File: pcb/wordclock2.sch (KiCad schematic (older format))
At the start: 42 parts

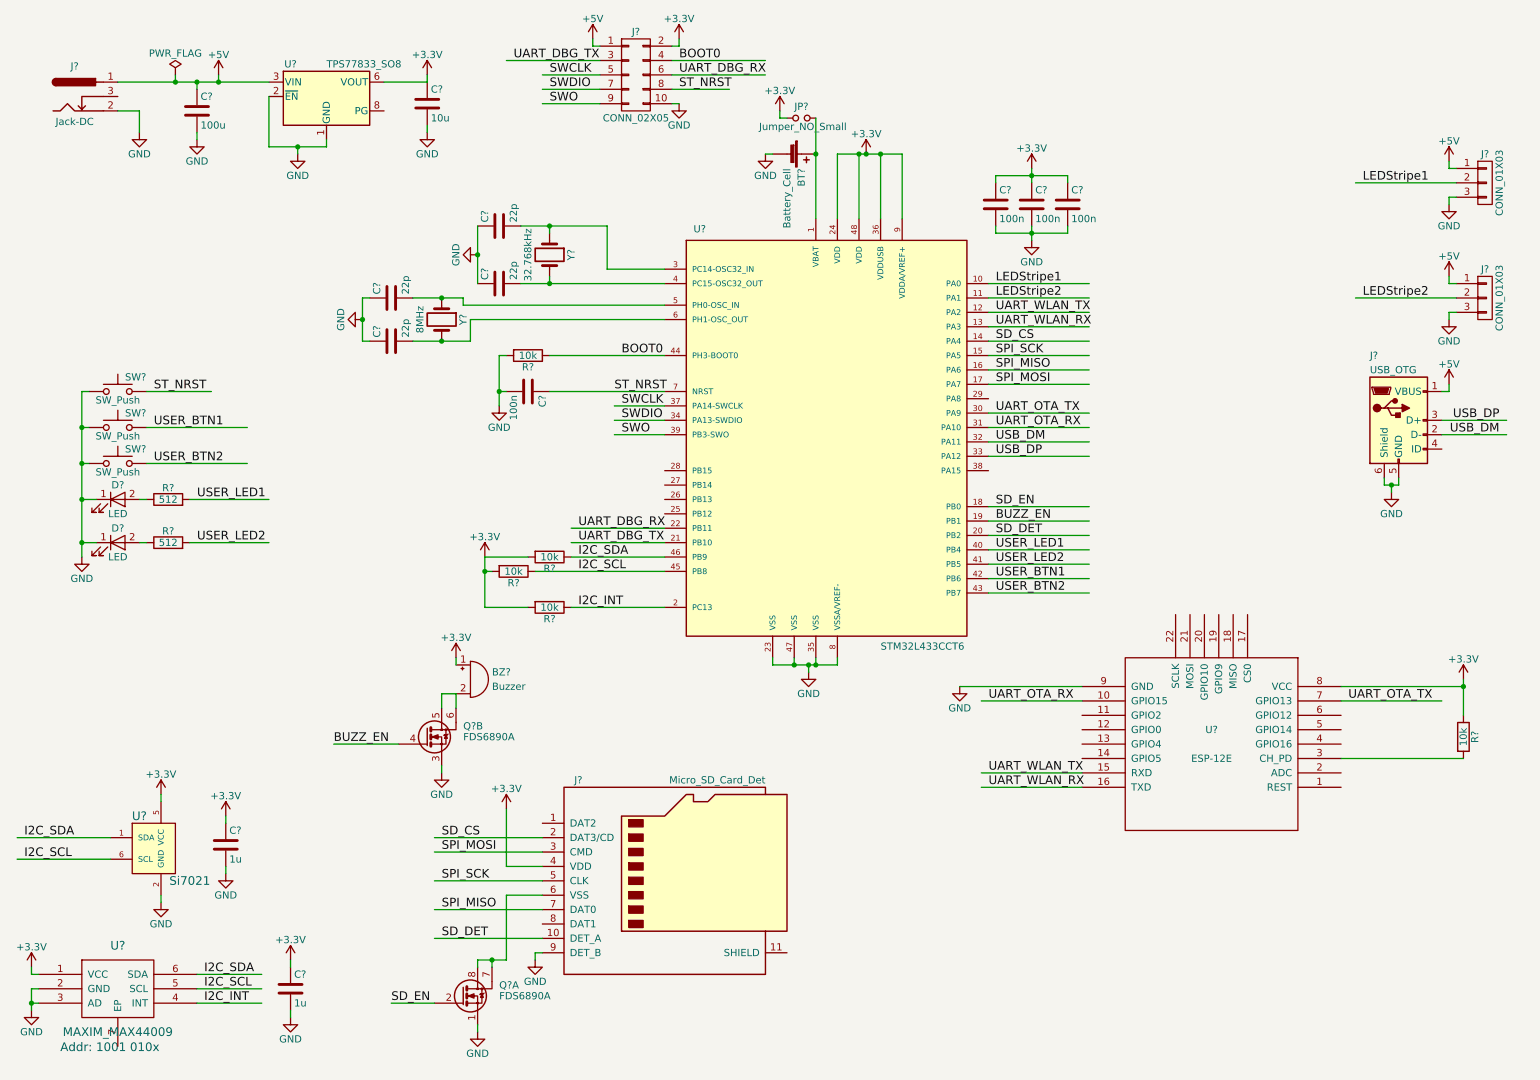
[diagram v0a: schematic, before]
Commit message: added datasheets
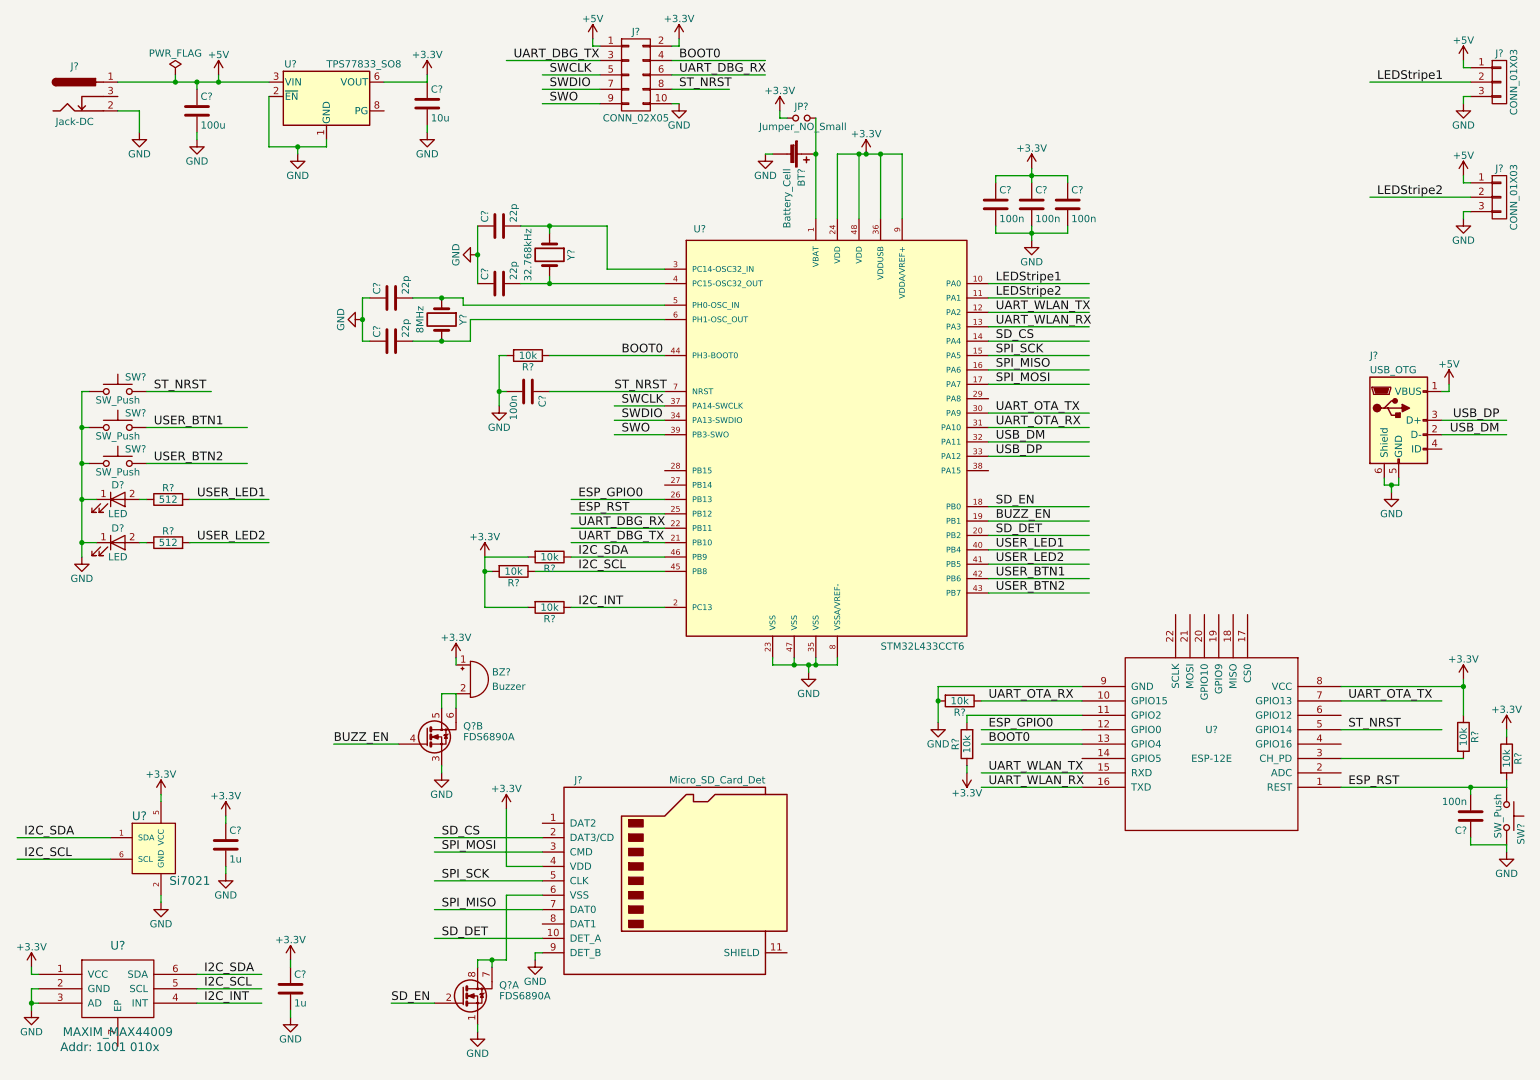
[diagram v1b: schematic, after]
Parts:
- added C?: 100n, symbol C
- added R? (x3): 10k, symbol R
- added SW?: SW_Push, symbol SW_Push
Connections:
- net labels added: ESP_GPIO0, ESP_RST
- wire segments 178 -> 194
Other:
- moved on the sheet: J?

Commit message: progress
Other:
- moved on the sheet: BZ?, Q?B

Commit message: progress
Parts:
- added R?: 10k, symbol R
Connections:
- wire segments 194 -> 197
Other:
- moved on the sheet: BZ?, Q?B
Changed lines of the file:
@@
 L Buzzer BZ?
 U 1 1 5983AD21
-P 3250 5150
-F 0 "BZ?" H 3400 5200 50  0000 L CNN
-F 1 "Buzzer" H 3400 5100 50  0000 L CNN
-F 2 "" V 3225 5250 50  0001 C CNN
-F 3 "" V 3225 5250 50  0001 C CNN
-	1    3250 5150
+P 1700 4850
+F 0 "BZ?" H 1850 4900 50  0000 L CNN
+F 1 "Buzzer" H 1850 4800 50  0000 L CNN
+F 2 "" V 1675 4950 50  0001 C CNN
+F 3 "" V 1675 4950 50  0001 C CNN
+	1    1700 4850
 	1    0    0    -1
 $EndComp
@@
 L FDS6890A Q?
 U 2 1 5984F828
-P 2950 5550
-F 0 "Q?" H 3200 5625 50  0000 L CNN
-F 1 "FDS6890A" H 3200 5550 50  0000 L CNN
-F 2 "Housings_SOIC:SOIC-8_3.9x4.9mm_Pitch1.27mm" H 3200 5475 50  0001 L CIN
-F 3 "" H 2950 5550 50  0001 L CNN
-	2    2950 5550
-	1    0    0    -1
-$EndComp
-Wire Wire Line
-	3150 5250 3050 5250
-Wire Wire Line
-	3050 5250 3050 5350
-Wire Wire Line
-	3150 5250 3150 5350
-Wire Wire Line
-	3050 5750 3050 5800
+P 1400 5250
+F 0 "Q?" H 1650 5325 50  0000 L CNN
+F 1 "FDS6890A" H 1650 5250 50  0000 L CNN
+F 2 "Housings_SOIC:SOIC-8_3.9x4.9mm_Pitch1.27mm" H 1650 5175 50  0001 L CIN
+F 3 "" H 1400 5250 50  0001 L CNN
+	2    1400 5250
+	1    0    0    -1
+$EndComp
+Wire Wire Line
+	1600 4950 1500 4950
+Wire Wire Line
+	1500 4950 1500 5050
+Wire Wire Line
+	1600 4950 1600 5050
+Wire Wire Line
+	1500 5450 1500 5500
 $Comp
 L GND #PWR029
 U 1 1 59850461
-P 3050 5800
-F 0 "#PWR029" H 3050 5550 50  0001 C CNN
-F 1 "GND" H 3050 5650 50  0000 C CNN
-F 2 "" H 3050 5800 50  0001 C CNN
-F 3 "" H 3050 5800 50  0001 C CNN
-	1    3050 5800
+P 1500 5500
+F 0 "#PWR029" H 1500 5250 50  0001 C CNN
+F 1 "GND" H 1500 5350 50  0000 C CNN
+F 2 "" H 1500 5500 50  0001 C CNN
+F 3 "" H 1500 5500 50  0001 C CNN
+	1    1500 5500
 	1    0    0    -1
 $EndComp
@@
 L +3.3V #PWR030
 U 1 1 59850E3B
-P 3150 5000
-F 0 "#PWR030" H 3150 4850 50  0001 C CNN
-F 1 "+3.3V" H 3150 5140 50  0000 C CNN
-F 2 "" H 3150 5000 50  0001 C CNN
-F 3 "" H 3150 5000 50  0001 C CNN
-	1    3150 5000
-	1    0    0    -1
-$EndComp
-Wire Wire Line
-	3150 5000 3150 5050
+P 1600 4700
+F 0 "#PWR030" H 1600 4550 50  0001 C CNN
+F 1 "+3.3V" H 1600 4840 50  0000 C CNN
+F 2 "" H 1600 4700 50  0001 C CNN
+F 3 "" H 1600 4700 50  0001 C CNN
+	1    1600 4700
+	1    0    0    -1
+$EndComp
+Wire Wire Line
+	1600 4700 1600 4750
 Wire Wire Line
 	3800 7050 4000 7050
@@
 L +3.3V #PWR032
 U 1 1 59852472
-P 4000 6000
-F 0 "#PWR032" H 4000 5850 50  0001 C CNN
-F 1 "+3.3V" H 4000 6140 50  0000 C CNN
-F 2 "" H 4000 6000 50  0001 C CNN
-F 3 "" H 4000 6000 50  0001 C CNN
-	1    4000 6000
-	1    0    0    -1
-$EndComp
-Wire Wire Line
-	4250 6400 4000 6400
-Wire Wire Line
-	4000 6400 4000 6000
+P 4000 5800
+F 0 "#PWR032" H 4000 5650 50  0001 C CNN
+F 1 "+3.3V" H 4000 5940 50  0000 C CNN
+F 2 "" H 4000 5800 50  0001 C CNN
+F 3 "" H 4000 5800 50  0001 C CNN
+	1    4000 5800
+	1    0    0    -1
+$EndComp
+Wire Wire Line
+	4000 6400 4250 6400
+Wire Wire Line
+	4000 5800 4000 6400
 Wire Wire Line
 	4250 6200 3500 6200
@@
 Wire Wire Line
 	7350 3050 8050 3050
-Text Label 2300 5600 0    60   ~ 0
+Text Label 750  5300 0    60   ~ 0
 BUZZ_EN
 Wire Wire Line
-	2750 5600 2300 5600
+	1200 5300 750  5300
 Text Label 3200 7350 0    60   ~ 0
 SD_EN
@@
 Wire Wire Line
 	10700 6250 10950 6250
+$Comp
+L R R?
+U 1 1 5988617A
+P 4150 6000
+F 0 "R?" V 4230 6000 50  0000 C CNN
+F 1 "10k" V 4150 6000 50  0000 C CNN
+F 2 "" V 4080 6000 50  0001 C CNN
+F 3 "" H 4150 6000 50  0001 C CNN
+	1    4150 6000
+	-1   0    0    1
+$EndComp
+Wire Wire Line
+	4150 5850 4150 5800
+Wire Wire Line
+	4150 5800 4000 5800
+Wire Wire Line
+	4150 6200 4150 6150
+Connection ~ 4150 6200
 $EndSCHEMATC

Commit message: annotated schematic
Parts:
- gave numbers to parts that had none: 47
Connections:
- wire segments 197 -> 199
- no-connect marks 0 -> 19

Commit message: progress
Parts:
- U4: footprint LQFP48 -> Housings_QFP:LQFP-48_7x7mm_Pitch0.5mm
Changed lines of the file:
@@
 F 0 "U1" H 1300 7550 60  0000 C CNN
 F 1 "MAXIM_MAX44009" H 1300 6950 60  0000 C CNN
-F 2 "" H 1400 7150 60  0000 C CNN
+F 2 "" H 1400 7150 60  0001 C CNN
 F 3 "" H 1400 7150 60  0000 C CNN
 	1    1300 7250
@@
 F 0 "U2" H 1450 6450 60  0000 C CNN
 F 1 "Si7021" H 1800 6000 60  0000 C CNN
-F 2 "" H 1600 6050 60  0000 C CNN
+F 2 "" H 1600 6050 60  0001 C CNN
 F 3 "" H 1600 6050 60  0000 C CNN
 	1    1550 6250
@@
 F 0 "U4" H 5300 4900 50  0000 L BNN
 F 1 "STM32L433CCT6" H 6600 2000 50  0000 L BNN
-F 2 "LQFP48" H 6200 3450 50  0001 C CIN
+F 2 "Housings_QFP:LQFP-48_7x7mm_Pitch0.5mm" H 6200 3450 50  0001 C CIN
 F 3 "" H 6400 3350 50  0001 C CNN
 	1    6150 3450

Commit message: progres, new footprint, datasheet
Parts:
- added R12: 1k, symbol R
- BZ1: footprint (none) -> wordclockFB:PKLCS1212E; Digi-Key (none) -> 490-4683-1-ND
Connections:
- wire segments 199 -> 201

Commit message: progress
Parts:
- BT1: footprint (none) -> Connect:CR2032H
- J1: footprint (none) -> Connect:BARREL_JACK
- J4: footprint (none) -> Connect:USB_Micro-B
- U2: footprint (none) -> wordclockFB:Si7021-A20
- U5: footprint (none) -> ESP8266:ESP-12E_SMD

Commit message: progress
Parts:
- U1: footprint (none) -> wordclockFB:MAX44009
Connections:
- wire segments 201 -> 202
